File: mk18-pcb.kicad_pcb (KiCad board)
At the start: 2 copper layers, 128.2 x 75 mm, 71 parts, among them T1 Conn_01x01_Socket, T10 Conn_01x01_Socket, T2 Conn_01x01_Socket, T3 Conn_01x01_Socket, T4 Conn_01x01_Socket, T5 Conn_01x01_Socket, T6 Conn_01x01_Socket, T7 Conn_01x01_Socket, T8 Conn_01x01_Socket, T9 Conn_01x01_Socket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

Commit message: final production version of 1.0 woooo
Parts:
- added AUDIO1: Conn_01x03_Socket, Connector_JST:JST_EH_B3B-EH-A_1x03_P2.50mm_Vertical, F.Cu at (215.8, 114.6)
- added G***: LOGO, ct-kicad:qmk-lite, F.Cu at (143.8, 140.4)
- added G***: LOGO, ct-kicad:qmk-lite, B.Cu at (143.8, 140.4)
- moved G*** 1.29 mm to (211.0, 135.4)
- moved G*** 1.22 mm to (210.9, 135.4)
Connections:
- RESET1 pad 1: reset -> GND
- RESET1 pad 2: GND -> reset
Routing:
- net GPIO22: track 34.1 -> 93.1 mm, vias 5 -> 17
- net reset: track 51.7 -> 55.7 mm
- net +3V3: track 358.6 -> 361.0 mm
- net GND: vias 199 -> 205
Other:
- board text added: "5V 3V GD"
- board text added: "AUDIO"
- board text added: "By Sf"
- board text added: "GND G22 3V3"
- board text added: "SPLIT"
- board text added: "SWDIO SWGND SWCLK"
- board text added: "v1.0"
- board text removed: "5 3.3 G"
- board text removed: "SPLIT v"

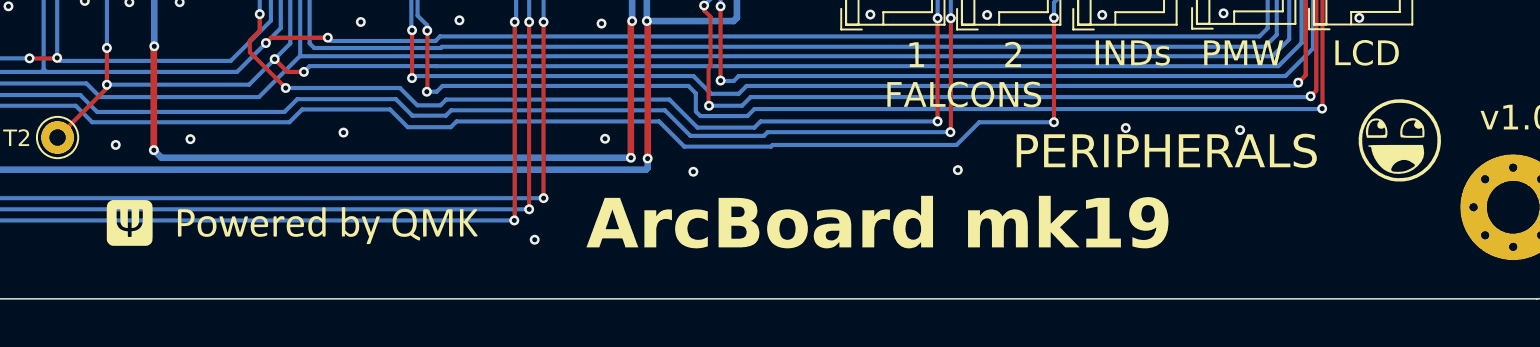
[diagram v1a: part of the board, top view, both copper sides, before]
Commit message: updating readme, tidied up schematic
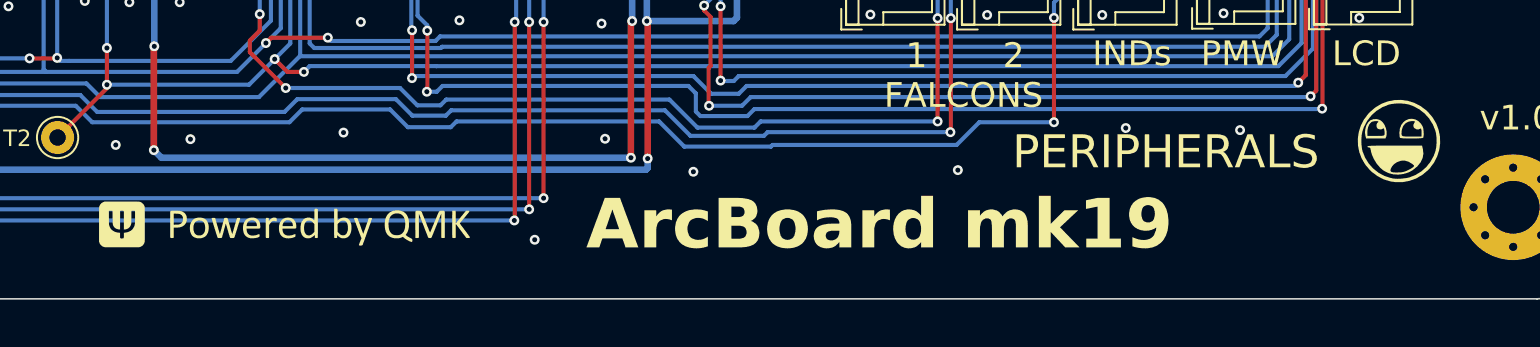
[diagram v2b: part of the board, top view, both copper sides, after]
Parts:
- removed G*** (x2): LOGO, ct-kicad:awesome-logo
- removed G*** (x2): LOGO, ct-kicad:qmk-lite
- added LOGO1: **REF, ct-kicad:awesome-logo, F.Cu at (211.0, 135.4)
- added LOGO2: **REF, ct-kicad:awesome-logo, B.Cu at (211.0, 135.4)
- added LOGO3: **REF, ct-kicad:qmk-lite, F.Cu at (143.3, 140.5)
- added LOGO4: **REF, ct-kicad:qmk-lite, B.Cu at (143.7, 140.6)
